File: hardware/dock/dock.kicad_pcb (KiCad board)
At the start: 2 copper layers, 46 parts, among them J2 Conn_01x05_Pin, J3 Conn_01x05_Pin, J6 Conn_01x05_Pin, J7 Conn_01x06, U1 TPS2116DRL, U2 TPS62162DSG, U4 TPD2EUSB30, U5 TPD2EUSB30, U6 TPD2EUSB30, U7 XIAO_nRF52840

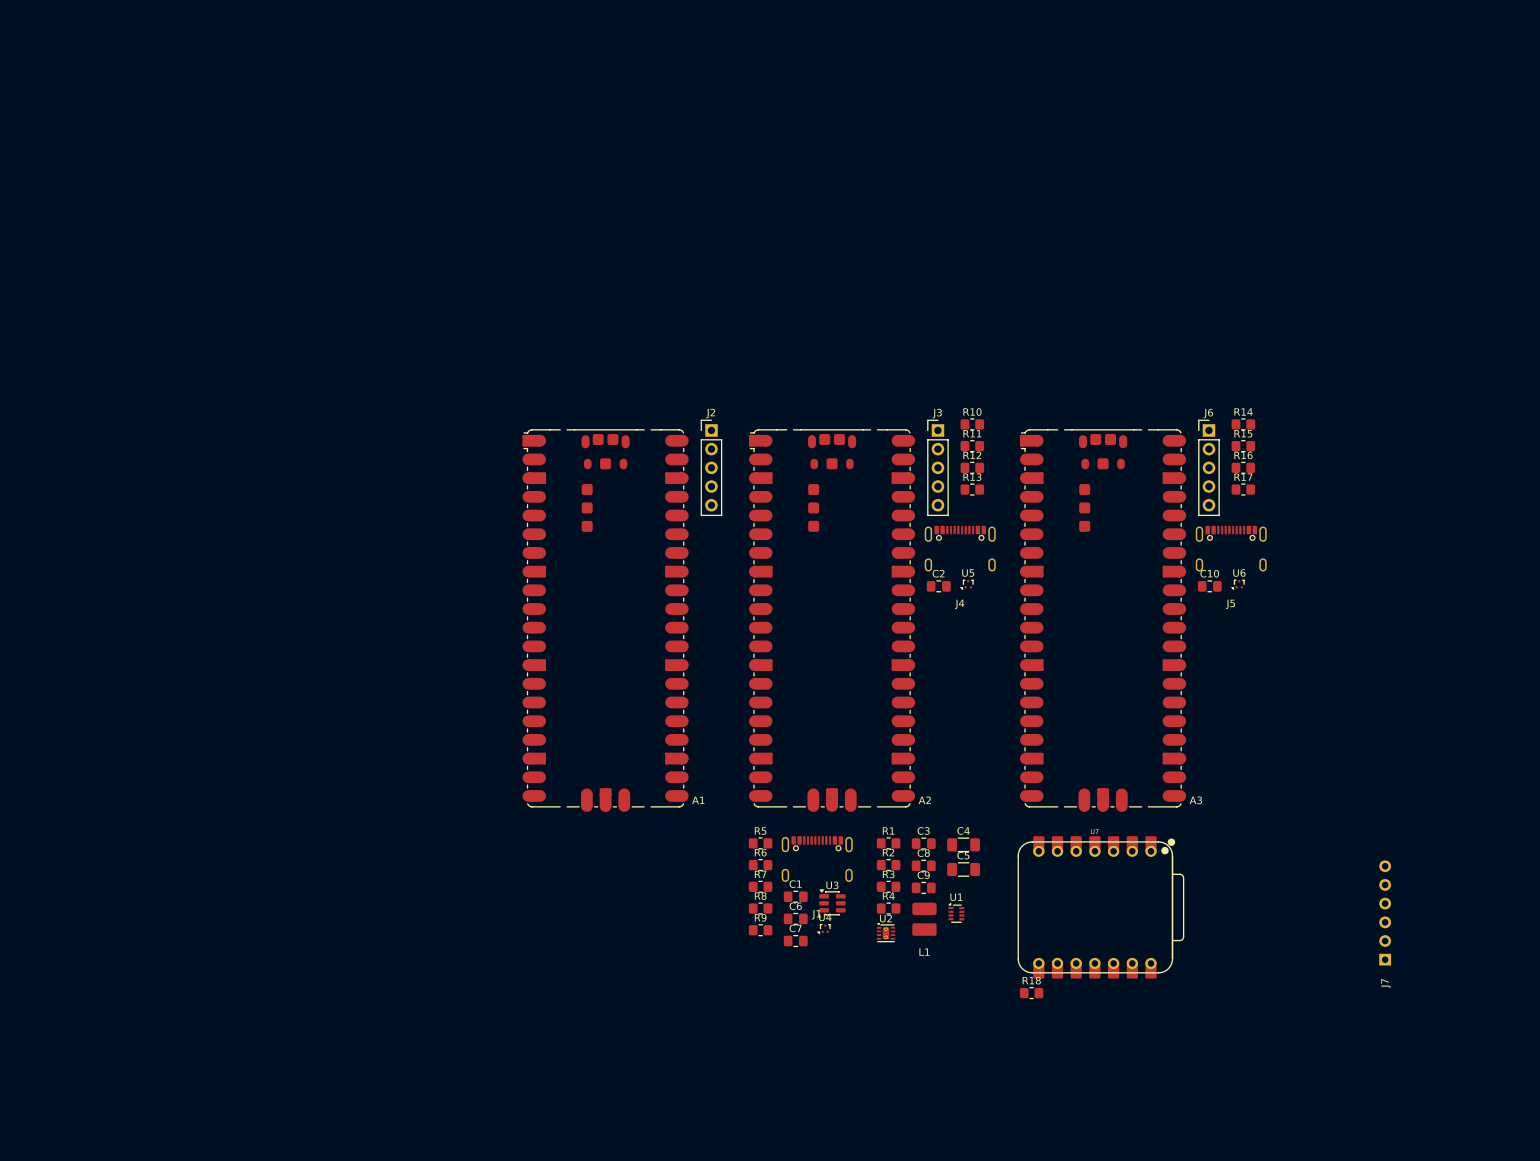
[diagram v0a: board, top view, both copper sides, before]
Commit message: Net classes, project lib tables, docs and datasheets; PCB synced
- Rename USB pairs to *_D_P/*_D_N; add Power and USB net classes
- Project-relative fp-lib-table and new sym-lib-table
- Pico values set to "Raspberry Pi Pico 2"; J1 symbol synced with library
- DESIGN.md/README: Pico 2 x3 + XIAO modules, TPS2116, pogo switch/ESD,
  VBUS/CC sensing, SWD pinout, resolved and open items
- Add TPS2552/2553, TPD2EUSB30 and P50 probe datasheets
- PCB updated from schematic (F8)

Co-Authored-By: Claude Opus 5.5 <noreply@anthropic.com>
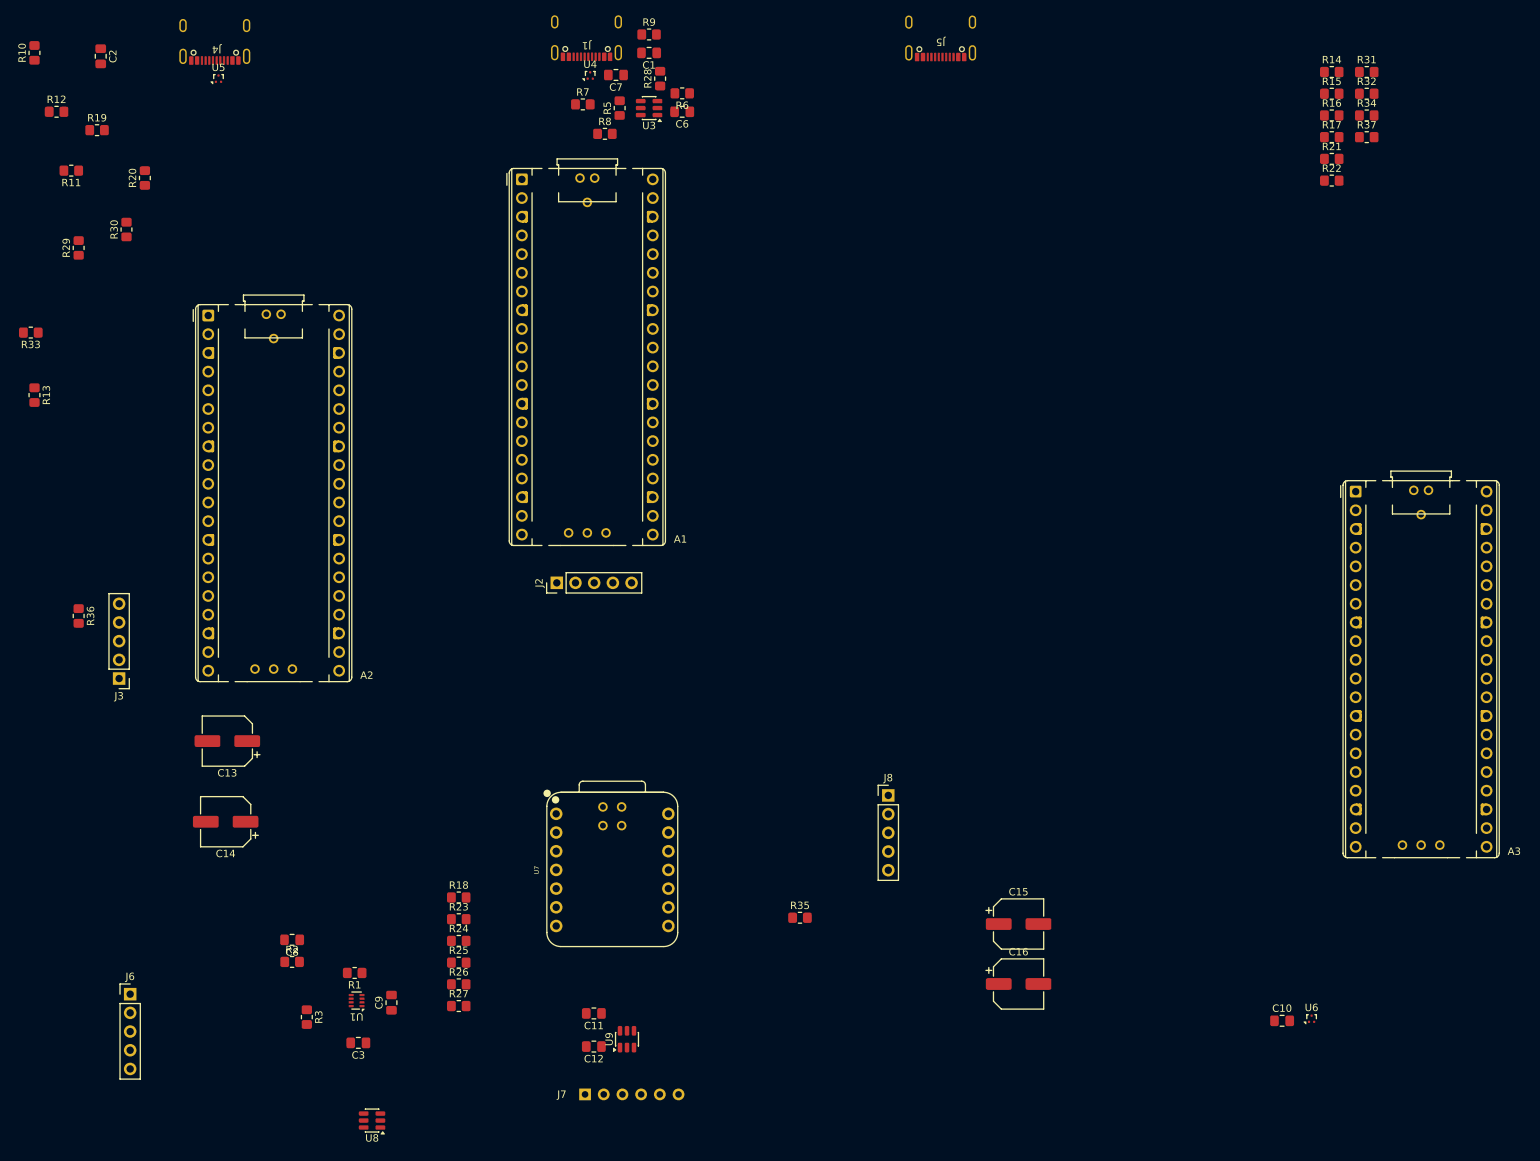
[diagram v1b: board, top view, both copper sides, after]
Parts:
- removed C4: 10uF, Capacitor_SMD:C_1206_3216Metric_Pad1.33x1.80mm_HandSolder
- removed C5: 22uF, Capacitor_SMD:C_1206_3216Metric_Pad1.33x1.80mm_HandSolder
- removed L1: 2.2uH, dock:FPI0302
- removed R4: 10k, Resistor_SMD:R_0805_2012Metric_Pad1.20x1.40mm_HandSolder
- removed U2: TPS62162DSG, Package_SON:Texas_DSG0008A_WSON-8-1EP_2x2mm_P0.5mm_EP0.9x1.6mm_ThermalVias
- added C11: 1uF, Capacitor_SMD:C_0805_2012Metric_Pad1.18x1.45mm_HandSolder, F.Cu at (113.0, 152.5)
- added C12: 1uF, Capacitor_SMD:C_0805_2012Metric_Pad1.18x1.45mm_HandSolder, F.Cu at (113.0, 157.0)
- added C13: 100uF, Capacitor_SMD:CP_Elec_6.3x7.7, F.Cu at (63.2, 115.5)
- added C14: 100uF, Capacitor_SMD:CP_Elec_6.3x7.7, F.Cu at (63.0, 126.5)
- added C15: 100uF, Capacitor_SMD:CP_Elec_6.3x7.7, F.Cu at (170.7, 140.3)
- added C16: 100uF, Capacitor_SMD:CP_Elec_6.3x7.7, F.Cu at (170.7, 148.5)
- added J8: Conn_01x05_Pin, Connector_PinHeader_2.54mm:PinHeader_1x05_P2.54mm_Vertical, F.Cu at (153.0, 122.9)
- added R19: 22k, Resistor_SMD:R_0805_2012Metric_Pad1.20x1.40mm_HandSolder, F.Cu at (45.5, 32.5)
- added R20: 33k, Resistor_SMD:R_0805_2012Metric_Pad1.20x1.40mm_HandSolder, F.Cu at (52.0, 39.0)
- added R21: 22k, Resistor_SMD:R_0805_2012Metric_Pad1.20x1.40mm_HandSolder, F.Cu at (213.2, 36.4)
- added R22: 33k, Resistor_SMD:R_0805_2012Metric_Pad1.20x1.40mm_HandSolder, F.Cu at (213.2, 39.4)
- added R23: 26.1k, Resistor_SMD:R_0805_2012Metric_Pad1.20x1.40mm_HandSolder, F.Cu at (94.6, 139.7)
- added R24: 10k, Resistor_SMD:R_0805_2012Metric_Pad1.20x1.40mm_HandSolder, F.Cu at (94.6, 142.6)
- added R25: 1k, Resistor_SMD:R_0805_2012Metric_Pad1.20x1.40mm_HandSolder, F.Cu at (94.6, 145.6)
- added R26: 1k, Resistor_SMD:R_0805_2012Metric_Pad1.20x1.40mm_HandSolder, F.Cu at (94.6, 148.5)
- added R27: 1k, Resistor_SMD:R_0805_2012Metric_Pad1.20x1.40mm_HandSolder, F.Cu at (94.6, 151.5)
- added R28: 100k, Resistor_SMD:R_0805_2012Metric_Pad1.20x1.40mm_HandSolder, F.Cu at (122.0, 25.5)
- added R29: 10k, Resistor_SMD:R_0805_2012Metric_Pad1.20x1.40mm_HandSolder, F.Cu at (43.0, 48.5)
- added R30: 10k, Resistor_SMD:R_0805_2012Metric_Pad1.20x1.40mm_HandSolder, F.Cu at (49.5, 46.0)
- added R31: 10k, Resistor_SMD:R_0805_2012Metric_Pad1.20x1.40mm_HandSolder, F.Cu at (218.0, 24.6)
- added R32: 10k, Resistor_SMD:R_0805_2012Metric_Pad1.20x1.40mm_HandSolder, F.Cu at (218.0, 27.6)
- added R33: 1k, Resistor_SMD:R_0805_2012Metric_Pad1.20x1.40mm_HandSolder, F.Cu at (36.5, 60.0)
- added R34: 1k, Resistor_SMD:R_0805_2012Metric_Pad1.20x1.40mm_HandSolder, F.Cu at (218.0, 30.5)
- added R35: 1k, Resistor_SMD:R_0805_2012Metric_Pad1.20x1.40mm_HandSolder, F.Cu at (141.0, 139.5)
- added R36: 10k, Resistor_SMD:R_0805_2012Metric_Pad1.20x1.40mm_HandSolder, F.Cu at (43.0, 98.5)
- added R37: 10k, Resistor_SMD:R_0805_2012Metric_Pad1.20x1.40mm_HandSolder, F.Cu at (218.0, 33.5)
- added U8: TPS2552DBVR, Package_TO_SOT_SMD:SOT-23-6, F.Cu at (82.9, 167.1)
- added U9: TPD4E1U06DBVR, Package_TO_SOT_SMD:SOT-23-6, F.Cu at (117.5, 156.0)
- A1, A2, A3: value RaspberryPi_Pico -> Raspberry Pi Pico 2; footprint Module:RaspberryPi_Pico_SMD -> dock:RaspberryPi_Pico2_Socket_Pogo
- U7: footprint xiao:XIAO-nRF52840-DIP -> dock:XIAO_nRF52840_Socket_Pogo
- moved J6 165.4 mm to (50.0, 149.9)
- moved R10 137.0 mm to (37.0, 22.0), turned to 90 degrees
- moved C2 134.7 mm to (46.0, 22.5), turned to -90 degrees
- moved R12 133.5 mm to (40.0, 30.0)
- moved R13 128.1 mm to (37.0, 68.5), turned to -90 degrees
- moved R11 128.0 mm to (42.0, 38.0), turned to 180 degrees
- moved U5 122.9 mm to (62.0, 25.5)
- moved R9 122.6 mm to (120.5, 19.5)
- moved U4 120.2 mm to (112.5, 25.1)
- moved C7 120.2 mm to (116.0, 25.0), turned to 180 degrees
- moved J4 119.7 mm to (61.5, 23.0), turned to 180 degrees
- moved C1 116.4 mm to (120.5, 22.0), turned to 180 degrees
- moved J3 116.2 mm to (48.5, 107.0), turned to 180 degrees
- moved J1 111.0 mm to (112.0, 22.5), turned to 180 degrees
- moved U3 110.9 mm to (120.5, 29.5), turned to 180 degrees
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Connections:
- net /HID_PERSONAL/USB_PERSONAL_DM renamed /HID_PERSONAL/USB_PERSONAL_D_N
- net /HID_PERSONAL/USB_PERSONAL_DP renamed /HID_PERSONAL/USB_PERSONAL_D_P
- net /HID_WORK/USB_WORK_DM renamed /HID_WORK/USB_WORK_D_N
- net /HID_WORK/USB_WORK_DP renamed /HID_WORK/USB_WORK_D_P
- net Net-(A2-RUN) renamed /HID_PERSONAL/RUN
- net Net-(A3-RUN) renamed /HID_WORK/RUN
- net Net-(J4-CC1_A5) renamed /HID_PERSONAL/CC1
- net Net-(J4-CC2_B5) renamed /HID_PERSONAL/CC2
- net Net-(J5-CC1_A5) renamed /HID_WORK/CC1
- net Net-(J5-CC2_B5) renamed /HID_WORK/CC2
- net USB_HOST_DM renamed USB_HOST_D_N
- net USB_HOST_DP renamed USB_HOST_D_P
- A1 pad 25: DOCK_3V3_GOOD -> HID_PERSONAL_RUN_CTRL
- A1 pad 26: unconnected-(A1-GPIO20-Pad26) -> POGO_5V_FAULT
- A1 pad 27: unconnected-(A1-GPIO21-Pad27) -> HID_WORK_RUN_CTRL
- A1 pad 29: unconnected-(A1-GPIO22-Pad29) -> BLE_RST_CTRL
- A1 pad 36: /RP2350_HOST/PICO_3V3 -> HOST_3V3
- A2 pad 1: HID_PERSONAL_TX -> HID_PERSONAL_RX
- A2 pad 2: HID_PERSONAL_RX -> HID_PERSONAL_TX
- A2 pad 31: unconnected-(A2-GPIO26_ADC0-Pad31) -> Net-(A2-GPIO26_ADC0)
- A2 pad 32: unconnected-(A2-GPIO27_ADC1-Pad32) -> Net-(A2-GPIO27_ADC1)
- A2 pad 4: ROLE_STRAP -> Net-(A2-GPIO2)
- A2 pad 6: unconnected-(A2-GPIO4-Pad6) -> Net-(A2-GPIO4)
- A3 pad 1: HID_WORK_TX -> HID_WORK_RX
- A3 pad 2: HID_WORK_RX -> HID_WORK_TX
- A3 pad 31: unconnected-(A3-GPIO26_ADC0-Pad31) -> Net-(A3-GPIO26_ADC0)
- A3 pad 32: unconnected-(A3-GPIO27_ADC1-Pad32) -> Net-(A3-GPIO27_ADC1)
- A3 pad 4: ROLE_STRAP -> Net-(A3-GPIO2)
- A3 pad 6: unconnected-(A3-GPIO4-Pad6) -> Net-(A3-GPIO4)
- J2 pad 5: /RP2350_HOST/PICO_3V3 -> HOST_3V3
- J7 pad 2: SYS_5V -> /BLE_BASE/POGO_5V
- J7 pad 3: Net-(J7-Pin_3) -> /BLE_BASE/POGO_DET_CONN
- J7 pad 4: Net-(J7-Pin_4) -> /BLE_BASE/POGO_RX_CONN
- J7 pad 5: Net-(J7-Pin_5) -> /BLE_BASE/POGO_TX_CONN
- R13 pad 1: ROLE_STRAP -> GND
- R13 pad 2: GND -> Net-(A2-GPIO2)
- R17 pad 1: ROLE_STRAP -> /HID_WORK/PICO_3V3
- R17 pad 2: /HID_WORK/PICO_3V3 -> Net-(A3-GPIO2)
- R18 pad 1: Net-(J7-Pin_3) -> /BLE_BASE/POGO_DET
- R18 pad 2: DOCK_3V3 -> /BLE_BASE/XIAO_3V3
- R3 pad 1: DOCK_3V3 -> HOST_3V3
- R6 pad 1: DOCK_3V3 -> HOST_3V3
- U7 pad 1: Net-(J7-Pin_5) -> /BLE_BASE/POGO_TX
- U7 pad 12: DOCK_3V3 -> /BLE_BASE/XIAO_3V3
- U7 pad 14: unconnected-(U7-5V_VBUS-Pad14)_1 -> SYS_5V
- U7 pad 2: Net-(J7-Pin_4) -> /BLE_BASE/POGO_RX
- U7 pad 3: Net-(J7-Pin_3) -> /BLE_BASE/POGO_DET
